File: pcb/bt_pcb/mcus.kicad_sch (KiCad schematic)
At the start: 32 parts, among them IC3 STM32H750VBT6, IC4 STM32H523CEU6, IC5 W25Q512JVEIM, J13 Conn_01x05, J14 Conn_01x05, J15 Conn_01x04, J16 Conn_01x04

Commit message: first notes
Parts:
- added R39, R40: 10k, Resistor_SMD:R_0603_1608Metric_Pad0.98x0.95mm_HandSolder, symbol Device:R
- renumbered C47 to C37, C48 to C38, C49 to C39, C50 to C40, C51 to C41, C52 to C42, C53 to C43, C54 to C44, C55 to C45, C56 to C46, C57 to C47, C58 to C48, C59 to C49, C60 to C50, C61 to C51, C62 to C52, C63 to C53, C64 to C54, C65 to C55, R40 to R41, R41 to R42, R42 to R43, R43 to R44
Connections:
- net GND: now also J13.3 (Pin_3), J14.3 (Pin_3), R39.1, R40.1; no longer IC3.94 (BOOT0), IC4.44 (BOOT0), J13.1 (Pin_1), J14.1 (Pin_1)
- net MCU1_DEB_SWCLK: now also J14.4 (Pin_4); no longer J14.3 (Pin_3)
- net MCU1_DEB_SWDIO: now also J14.2 (Pin_2); no longer J14.4 (Pin_4)
- net MCU1_NRST: now also J14.1 (Pin_1); no longer J14.2 (Pin_2)
- net MCU2_DEB_SWCLK: now also J13.4 (Pin_4); no longer J13.3 (Pin_3)
- net MCU2_DEB_SWDIO: now also J13.2 (Pin_2); no longer J13.4 (Pin_4)
- net MCU2_NRST: now also J13.1 (Pin_1); no longer J13.2 (Pin_2)
- new net: IC4.44 (BOOT0), R40.2
- new net: IC3.94 (BOOT0), R39.2

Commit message: first reiteration
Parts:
- J13, J14: footprint Connector_PinHeader_2.54mm:PinHeader_1x05_P2.54mm_Vertical -> Connector_JST:JST_PH_B5B-PH-K_1x05_P2.00mm_Vertical
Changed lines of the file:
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@@
 			)
 		)
-		(property "Footprint" "Connector_PinHeader_2.54mm:PinHeader_1x05_P2.54mm_Vertical"
+		(property "Footprint" "Connector_JST:JST_PH_B5B-PH-K_1x05_P2.00mm_Vertical"
 			(at 193.04 49.53 0)
 			(effects
@@
 			)
 		)
-		(property "Footprint" "Connector_PinHeader_2.54mm:PinHeader_1x05_P2.54mm_Vertical"
+		(property "Footprint" "Connector_JST:JST_PH_B5B-PH-K_1x05_P2.00mm_Vertical"
 			(at 276.86 44.45 0)
 			(effects

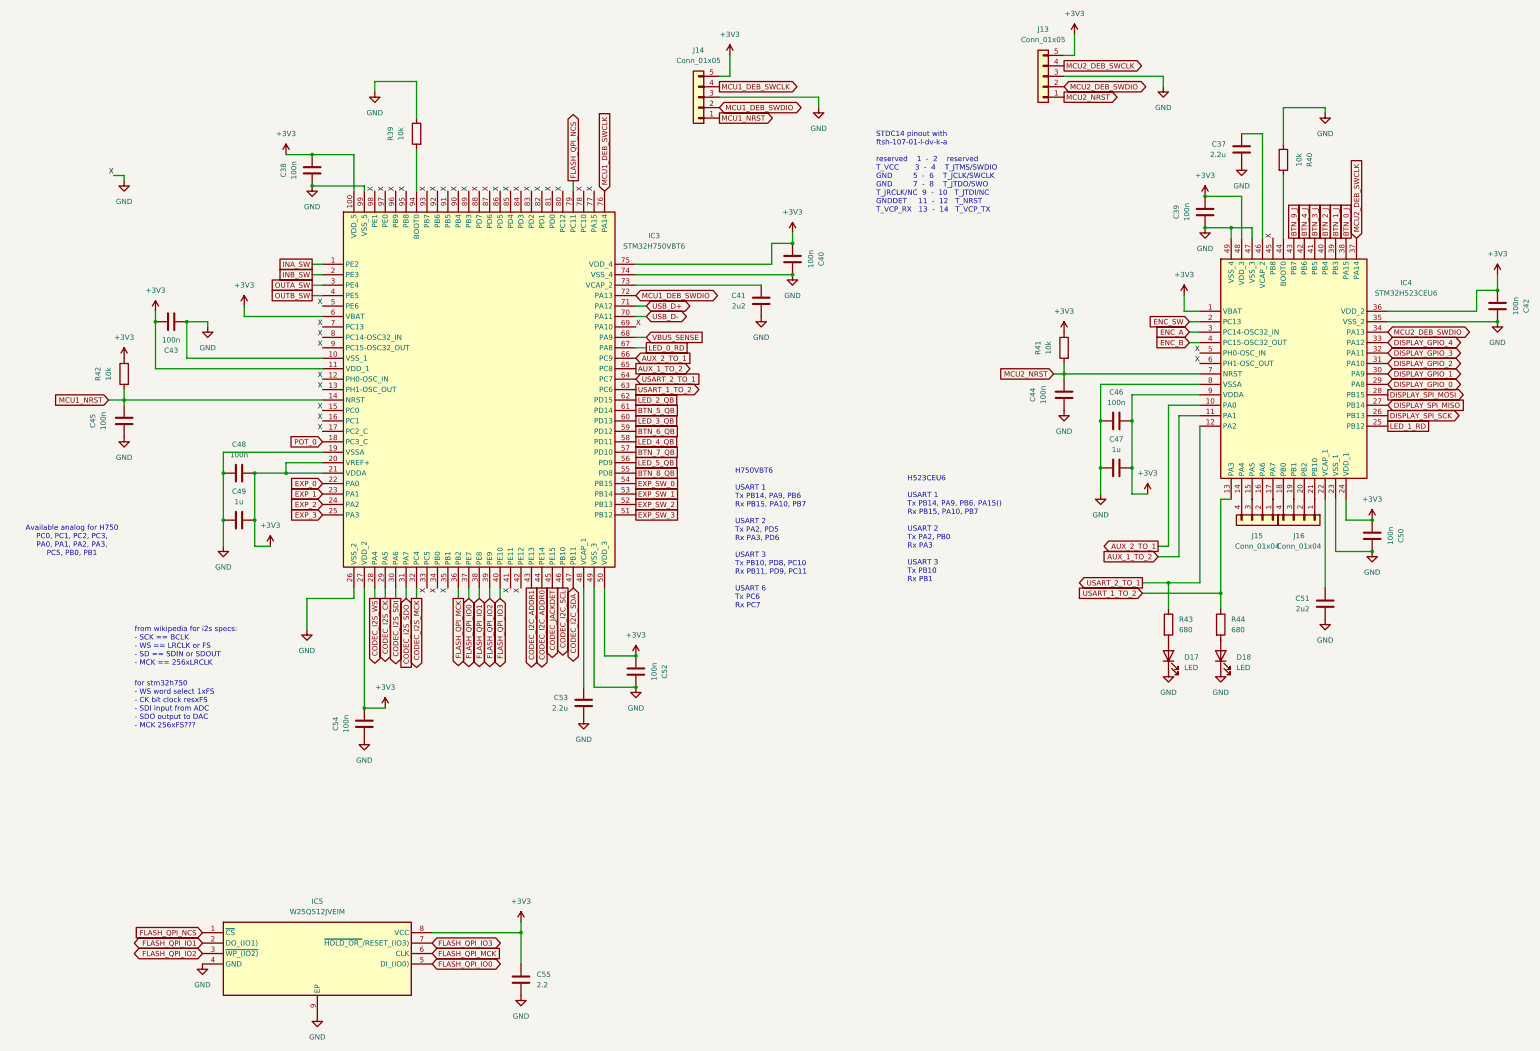
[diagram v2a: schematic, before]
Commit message: doing pcb from scratch again
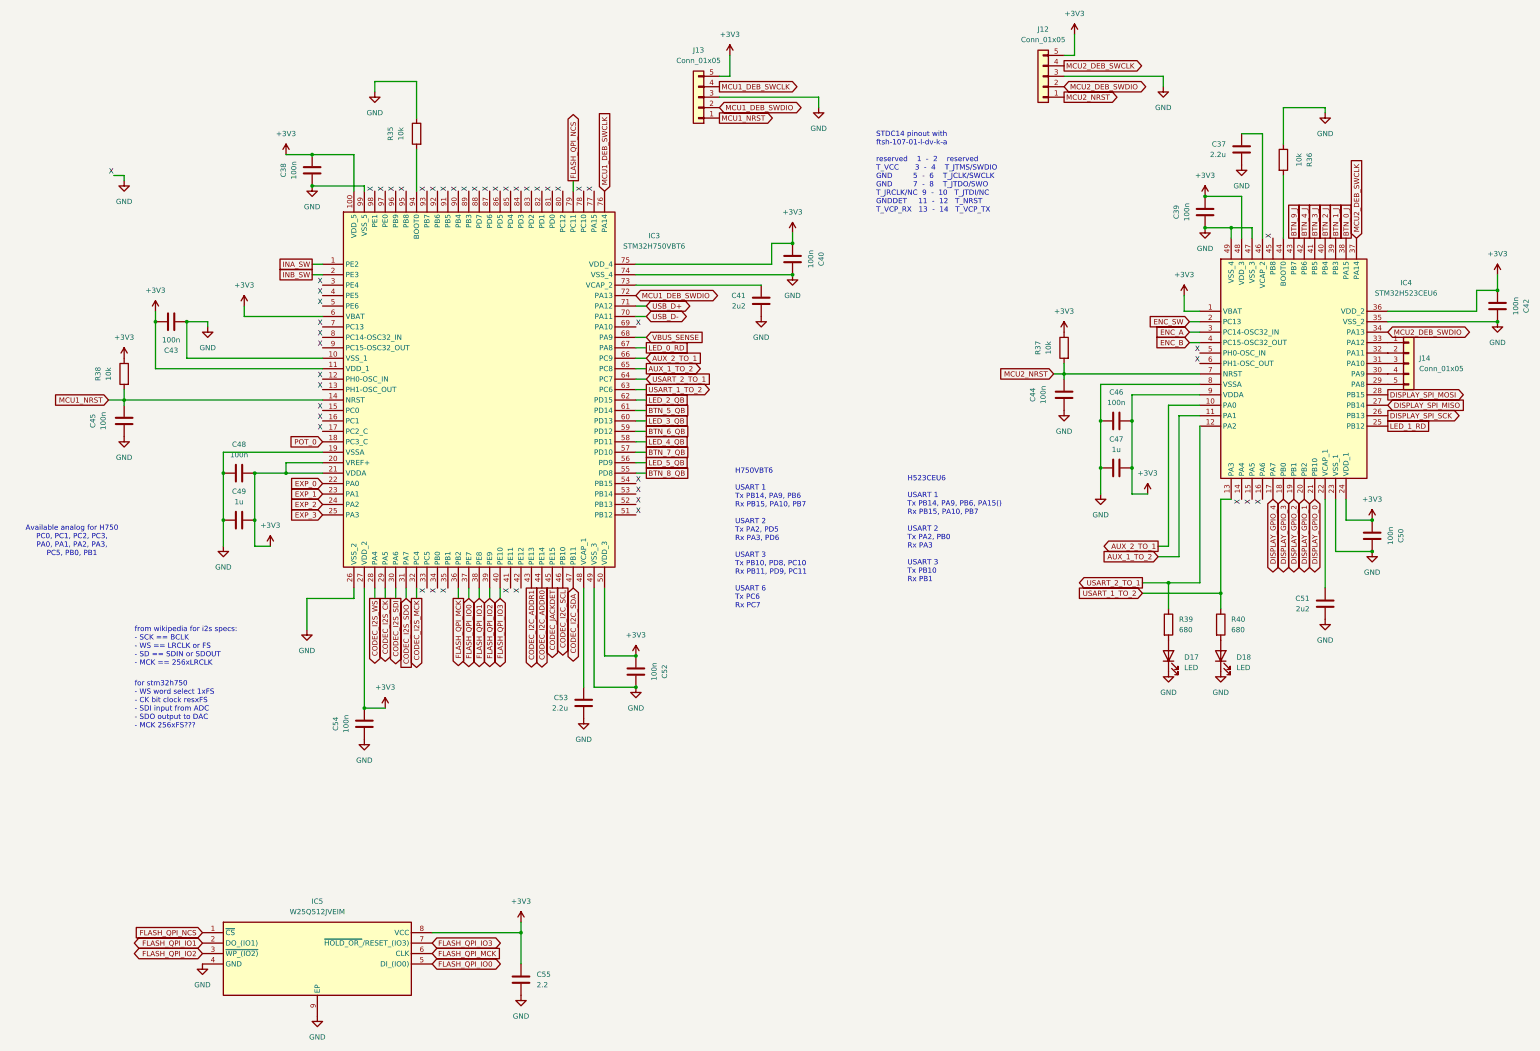
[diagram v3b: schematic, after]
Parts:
- removed J15, J16: Conn_01x04, Connector_PinHeader_2.54mm:PinHeader_1x04_P2.54mm_Vertical, symbol Connector_Generic:Conn_01x04
- added J14: Conn_01x05, Connector_JST:JST_PH_B5B-PH-K_1x05_P2.00mm_Vertical, symbol Connector_Generic:Conn_01x05
- renumbered J13 to J12, J14 to J13, R39 to R35, R40 to R36, R41 to R37, R42 to R38, R43 to R39, R44 to R40
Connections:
- net EXP_SW_0 is gone; now on net GND: IC3.54 (PB15)
- net EXP_SW_1 is gone; now on net GND: IC3.53 (PB14)
- net EXP_SW_2 is gone; now on net GND: IC3.52 (PB13)
- net EXP_SW_3 is gone; now on net GND: IC3.51 (PB12)
- net OUTA_SW is gone; now on net GND: IC3.3 (PE4)
- net OUTB_SW is gone; now on net GND: IC3.4 (PE5)
- net DISPLAY_GPIO_0: now also IC4.21 (PB10); no longer IC4.29 (PA8)
- net DISPLAY_GPIO_1: now also IC4.20 (PB2); no longer IC4.30 (PA9)
- net DISPLAY_GPIO_2: now also IC4.19 (PB1); no longer IC4.31 (PA10)
- net DISPLAY_GPIO_3: now also IC4.18 (PB0); no longer IC4.32 (PA11)
- net DISPLAY_GPIO_4: now also IC4.17 (PA7); no longer IC4.33 (PA12)
- net GND: now also IC4.14 (PA4), IC4.15 (PA5), IC4.16 (PA6)
- new net: IC4.29 (PA8), J14.5 (Pin_5)
- new net: IC4.30 (PA9), J14.4 (Pin_4)
- new net: IC4.31 (PA10), J14.3 (Pin_3)
- new net: IC4.32 (PA11), J14.2 (Pin_2)
- new net: IC4.33 (PA12), J14.1 (Pin_1)

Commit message: routing stuff
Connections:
- net DISPLAY_GPIO_0: now also IC4.17 (PA7); no longer IC4.21 (PB10)
- net DISPLAY_GPIO_1: now also IC4.18 (PB0); no longer IC4.20 (PB2)
- net DISPLAY_GPIO_3: now also IC4.20 (PB2); no longer IC4.18 (PB0)
- net DISPLAY_GPIO_4: now also IC4.21 (PB10); no longer IC4.17 (PA7)

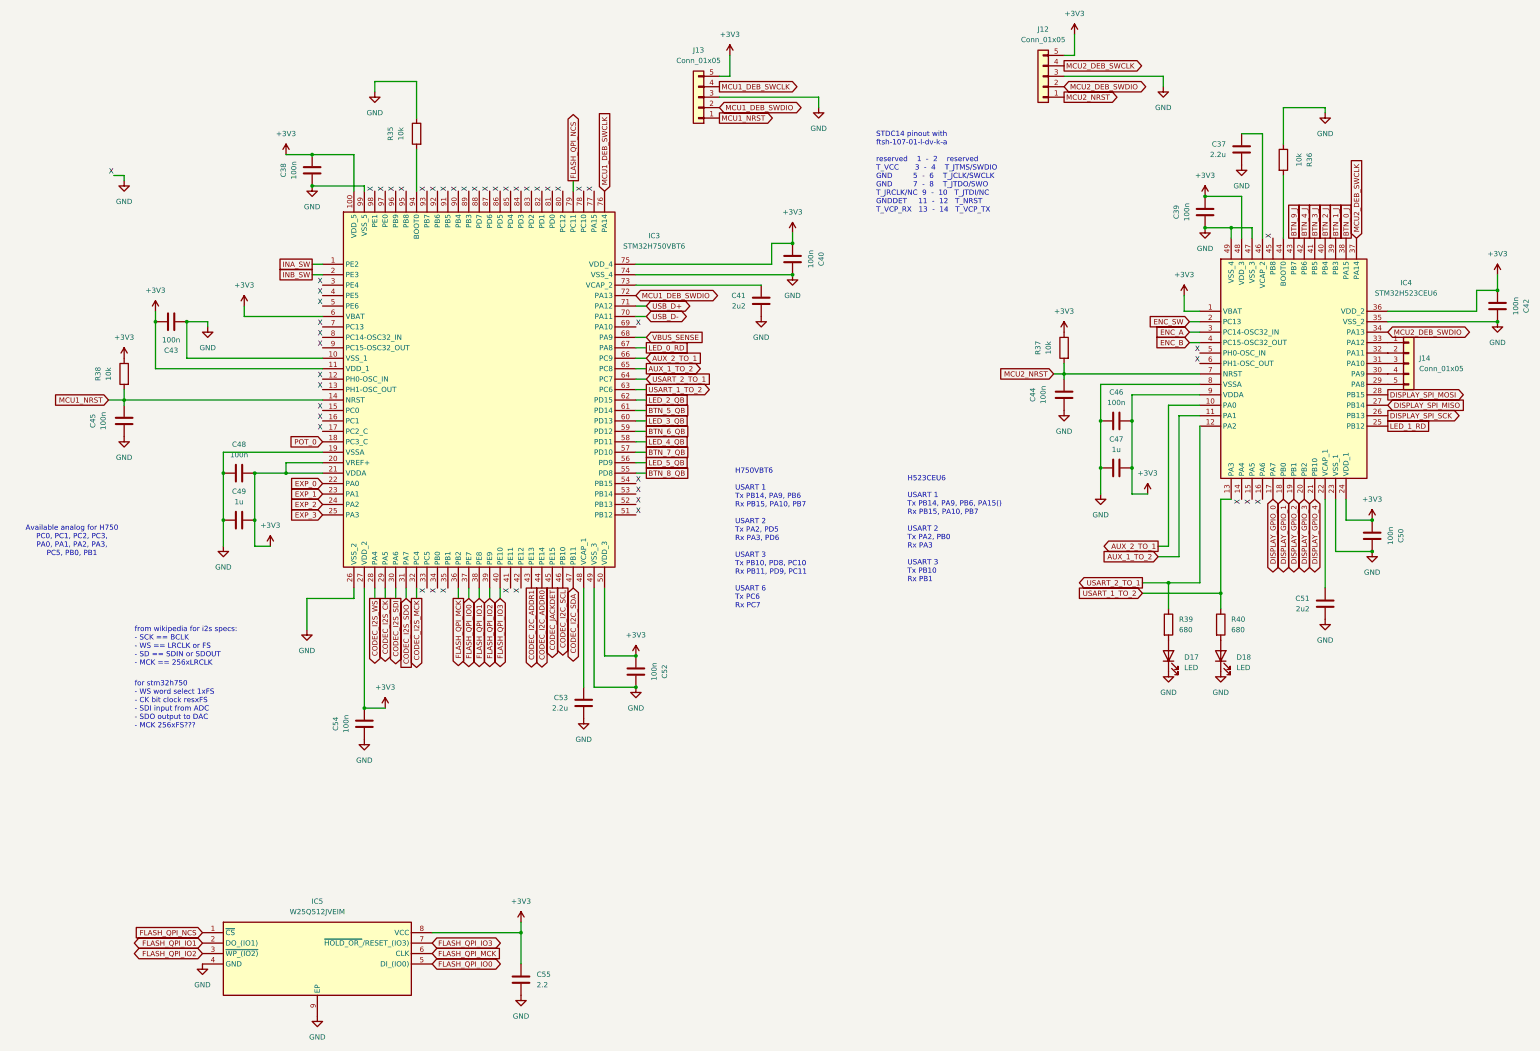
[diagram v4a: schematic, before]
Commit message: redo of power supply
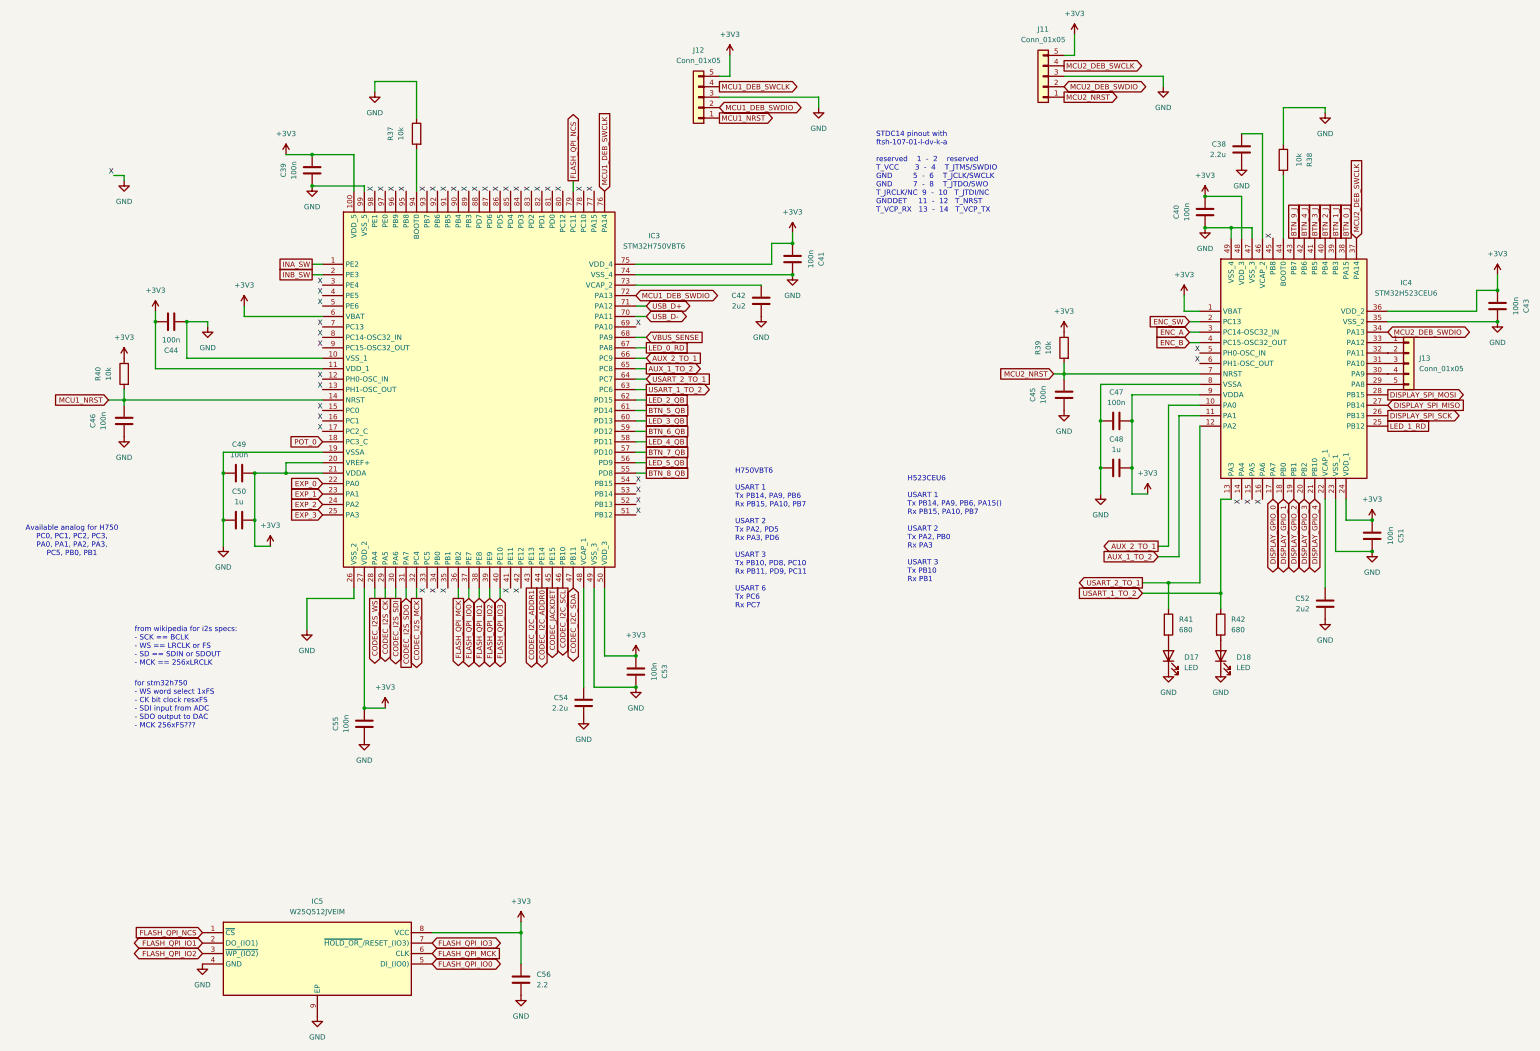
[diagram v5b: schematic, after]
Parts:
- renumbered C37 to C38, C38 to C39, C39 to C40, C40 to C41, C41 to C42, C42 to C43, C43 to C44, C44 to C45, C45 to C46, C46 to C47, C47 to C48, C48 to C49, C49 to C50, C50 to C51, C51 to C52, C52 to C53, C53 to C54, C54 to C55, C55 to C56, J12 to J11, J13 to J12, J14 to J13, R35 to R37, R36 to R38, R37 to R39, R38 to R40, R39 to R41, R40 to R42

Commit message: made a bom
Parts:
- added TP1, TP2, TP3, TP4: TestPoint, TestPoint:TestPoint_Pad_D1.0mm, symbol Connector:TestPoint
- IC3, IC4, J11, J12, J13: now left out of the parts list
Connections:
- net GND: no longer IC3.12 (PH0-OSC_IN), IC3.13 (PH1-OSC_OUT), IC3.15 (PC0), IC3.16 (PC1), IC3.17 (PC2_C), IC3.3 (PE4), IC3.33 (PC5), IC3.34 (PB0), IC3.35 (PB1), IC3.4 (PE5), IC3.41 (PE11), IC3.42 (PE12), IC3.5 (PE6), IC3.51 (PB12), IC3.52 (PB13), IC3.53 (PB14), IC3.54 (PB15), IC3.69 (PA10), IC3.7 (PC13), IC3.77 (PA15), IC3.78 (PC10), IC3.8 (PC14-OSC32_IN), IC3.80 (PC12), IC3.81 (PD0), IC3.82 (PD1), IC3.83 (PD2), IC3.84 (PD3), IC3.85 (PD4), IC3.86 (PD5), IC3.87 (PD6), IC3.88 (PD7), IC3.89 (PB3), IC3.9 (PC15-OSC32_OUT), IC3.90 (PB4), IC3.91 (PB5), IC3.92 (PB6), IC3.93 (PB7), IC3.95 (PB8), IC3.96 (PB9), IC3.97 (PE0), IC3.98 (PE1), IC4.14 (PA4), IC4.15 (PA5), IC4.16 (PA6), IC4.45 (PB8), IC4.5 (PH0-OSC_IN), IC4.6 (PH1-OSC_OUT)
- new net: IC3.85 (PD4), TP2.1
- new net: IC3.86 (PD5), TP1.1
- new net: IC3.84 (PD3), TP3.1
- new net: IC3.83 (PD2), TP4.1
- no-connect marks 0 -> 43

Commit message: updated and pretty bom
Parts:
- C56: value 2.2 -> 2.2u
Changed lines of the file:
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@@
 			)
 		)
-		(property "Value" "2.2"
+		(property "Value" "2.2u"
 			(at 153.67 265.43 0)
 			(effects

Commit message: seeing the end of the tunnel
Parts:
- C42, C52: value 2u2 -> 2.2u
- renumbered J11 to J12, J12 to J13, J13 to J14
